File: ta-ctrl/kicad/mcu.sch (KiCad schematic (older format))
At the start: 11 parts, among them U6 MSP430FR5994IPM, Y1 Crystal, Y2 Crystal

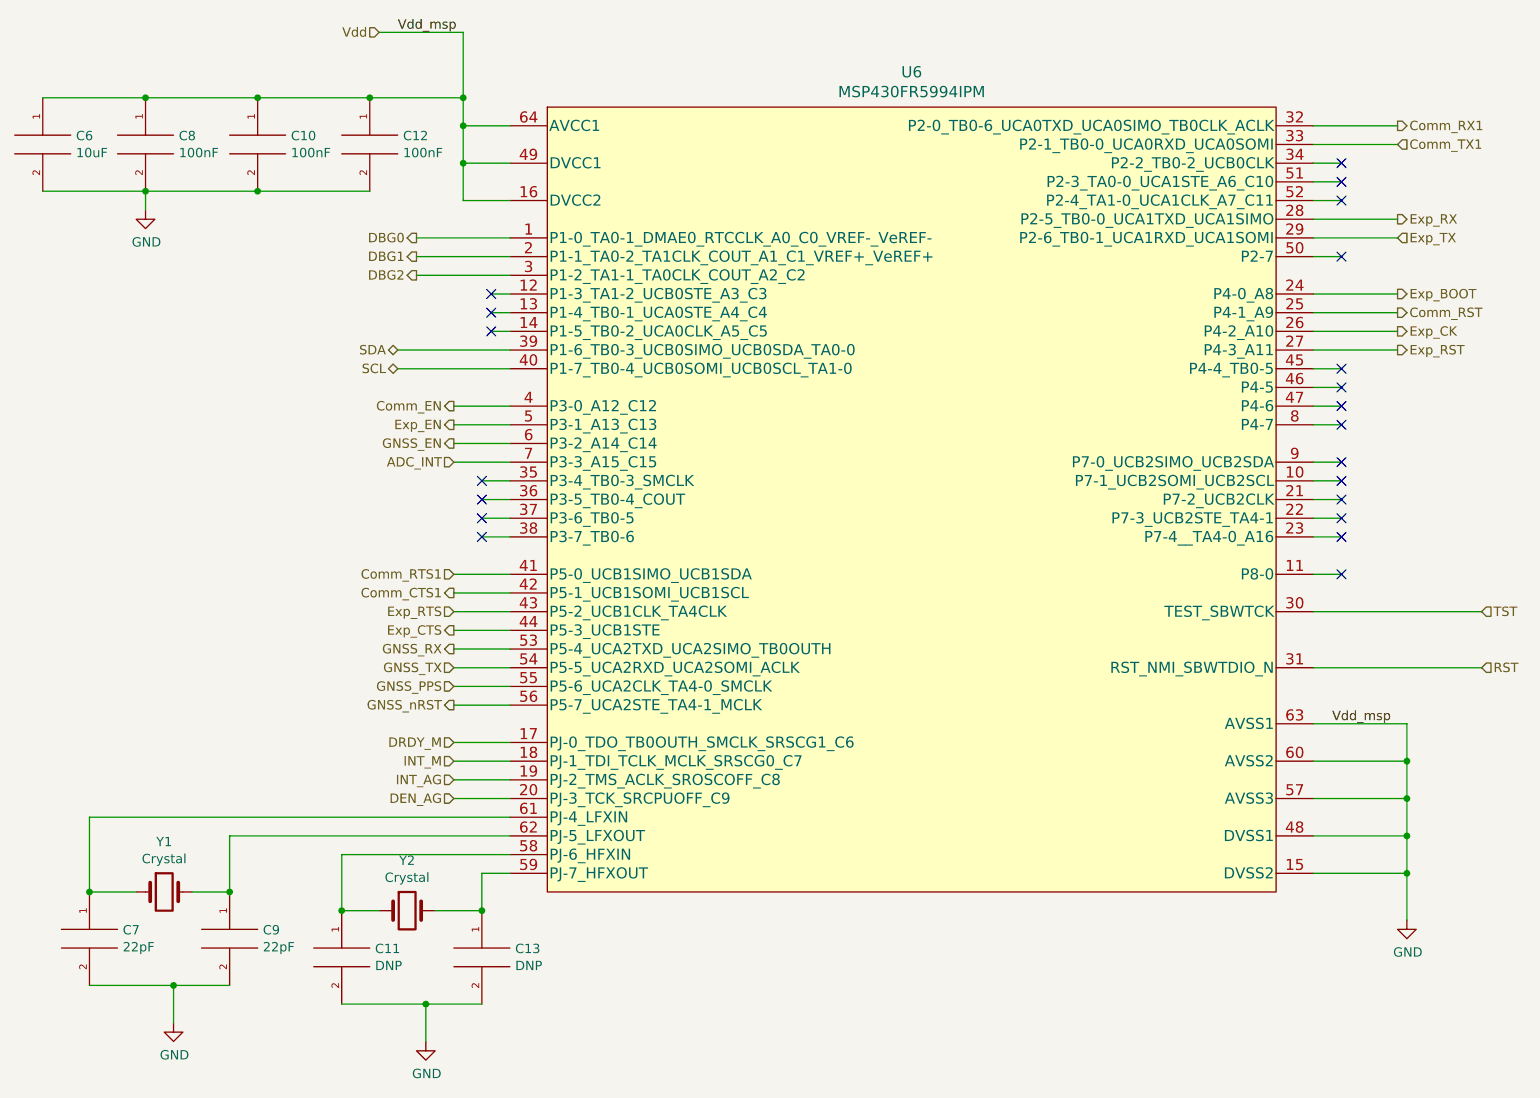
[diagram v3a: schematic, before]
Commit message: updated and checked all footprints, added a diode too
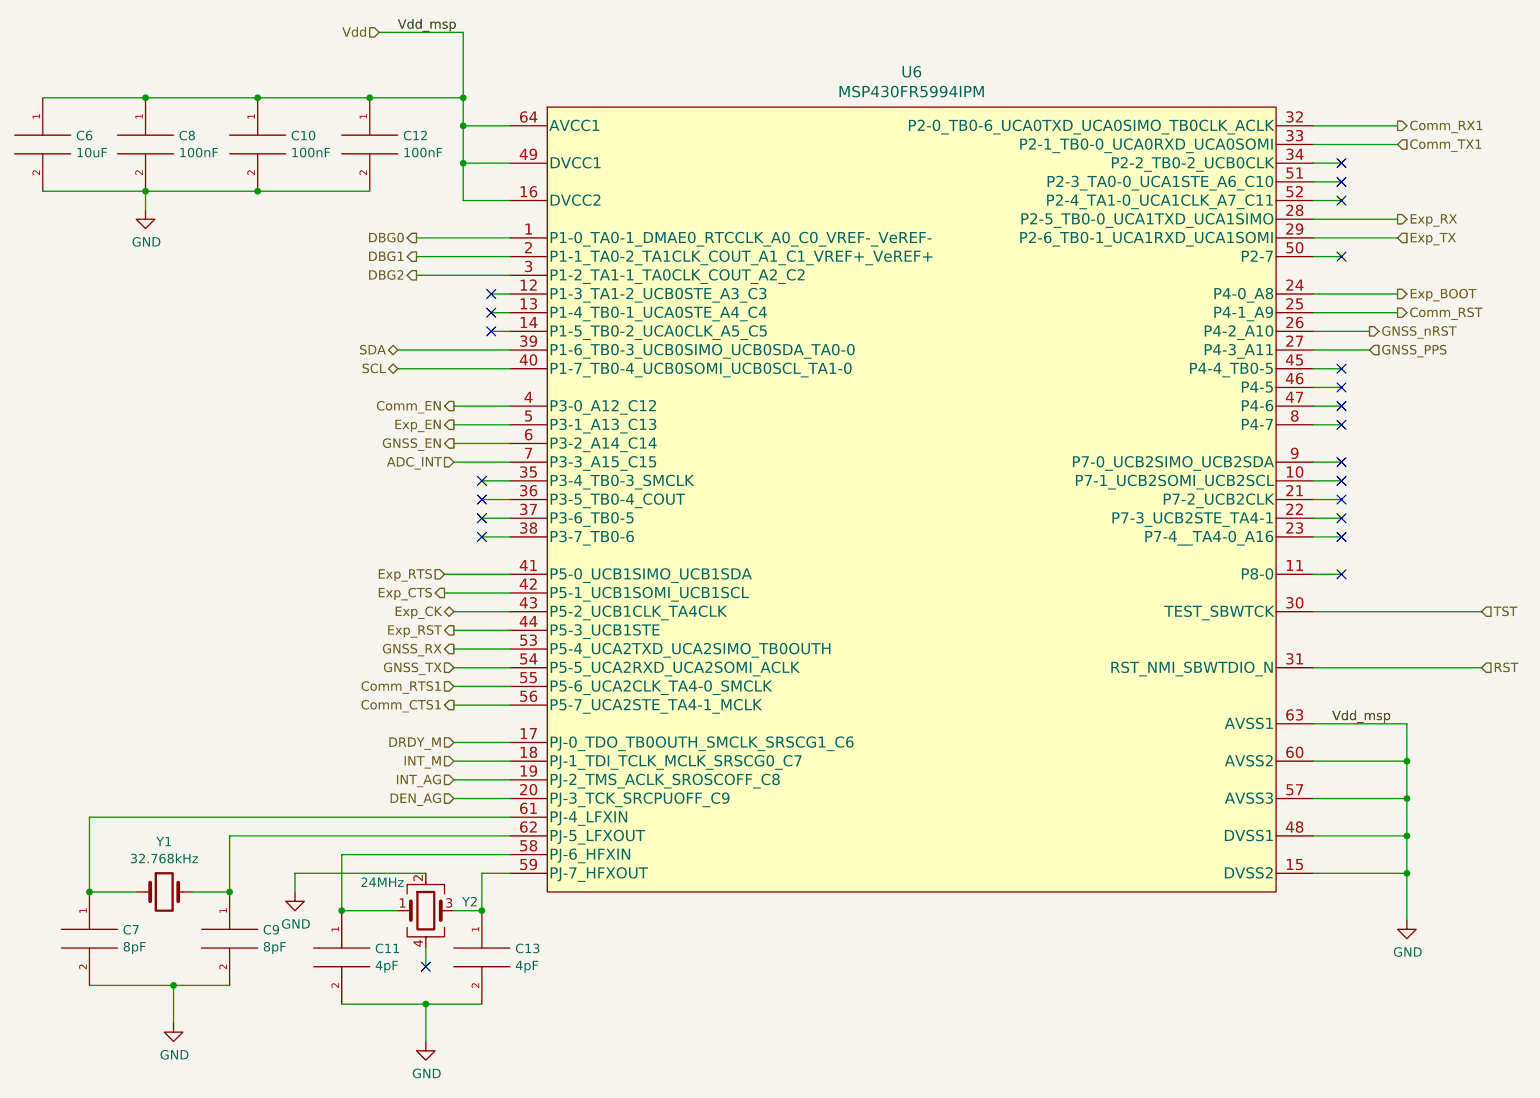
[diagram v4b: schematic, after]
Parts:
- removed Y2: Crystal, symbol Device:Crystal
- added Y2: 24MHz, ta-ctrl:ECX-1247, symbol Device:Crystal_GND24
- C10, C12, C6, C8: footprint (none) -> ta-ctrl:C_0603_1608Metric_ctrl_cpy
- C11, C13: value DNP -> 4pF; footprint (none) -> ta-ctrl:C_0402_1005Metric
- C7, C9: value 22pF -> 8pF; footprint (none) -> ta-ctrl:C_0402_1005Metric
- Y1: value Crystal -> 32.768kHz; footprint (none) -> ta-ctrl:ECS327934QSTR
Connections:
- net Comm_CTS1: now also U6.56 (P5-7_UCA2STE_TA4-1_MCLK); no longer U6.42 (P5-1_UCB1SOMI_UCB1SCL)
- net Comm_RTS1: now also U6.55 (P5-6_UCA2CLK_TA4-0_SMCLK); no longer U6.41 (P5-0_UCB1SIMO_UCB1SDA)
- net Exp_CK: now also U6.43 (P5-2_UCB1CLK_TA4CLK); no longer U6.26 (P4-2_A10)
- net Exp_CTS: now also U6.42 (P5-1_UCB1SOMI_UCB1SCL); no longer U6.44 (P5-3_UCB1STE)
- net Exp_RST: now also U6.44 (P5-3_UCB1STE); no longer U6.27 (P4-3_A11)
- net Exp_RTS: now also U6.41 (P5-0_UCB1SIMO_UCB1SDA); no longer U6.43 (P5-2_UCB1CLK_TA4CLK)
- net GND: now also Y2.2
- net GNSS_PPS: now also U6.27 (P4-3_A11); no longer U6.55 (P5-6_UCA2CLK_TA4-0_SMCLK)
- net GNSS_nRST: now also U6.26 (P4-2_A10); no longer U6.56 (P5-7_UCA2STE_TA4-1_MCLK)
- net at C11.1, U6.58 (PJ-6_HFXIN): now also Y2.1
- net at C13.1, U6.59 (PJ-7_HFXOUT): now also Y2.3
- no-connect marks 21 -> 22
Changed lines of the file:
@@
 Vdd_msp
 $Comp
-L power:GND #PWR021
+L power:GND #PWR023
 U 1 1 5F18B739
 P 8150 5800
-F 0 "#PWR021" H 8150 5550 50  0001 C CNN
+F 0 "#PWR023" H 8150 5550 50  0001 C CNN
 F 1 "GND" H 8155 5627 50  0000 C CNN
 F 2 "" H 8150 5800 50  0001 C CNN
@@
 F 0 "C8" H 1578 1696 50  0000 L CNN
 F 1 "100nF" H 1578 1605 50  0000 L CNN
-F 2 "" H 1400 1650 50  0001 C CNN
+F 2 "ta-ctrl:C_0603_1608Metric_ctrl_cpy" H 1400 1650 50  0001 C CNN
 F 3 "~" H 1400 1650 50  0001 C CNN
 	1    1400 1650
@@
 F 0 "C10" H 2178 1696 50  0000 L CNN
 F 1 "100nF" H 2178 1605 50  0000 L CNN
-F 2 "" H 2000 1650 50  0001 C CNN
+F 2 "ta-ctrl:C_0603_1608Metric_ctrl_cpy" H 2000 1650 50  0001 C CNN
 F 3 "~" H 2000 1650 50  0001 C CNN
 	1    2000 1650
@@
 F 0 "C12" H 2778 1696 50  0000 L CNN
 F 1 "100nF" H 2778 1605 50  0000 L CNN
-F 2 "" H 2600 1650 50  0001 C CNN
+F 2 "ta-ctrl:C_0603_1608Metric_ctrl_cpy" H 2600 1650 50  0001 C CNN
 F 3 "~" H 2600 1650 50  0001 C CNN
 	1    2600 1650
@@
 $EndComp
 $Comp
-L power:GND #PWR018
+L power:GND #PWR019
 U 1 1 5F18D1CF
 P 1400 2000
-F 0 "#PWR018" H 1400 1750 50  0001 C CNN
+F 0 "#PWR019" H 1400 1750 50  0001 C CNN
 F 1 "GND" H 1405 1827 50  0000 C CNN
 F 2 "" H 1400 2000 50  0001 C CNN
@@
 F 0 "C6" H 1028 1696 50  0000 L CNN
 F 1 "10uF" H 1028 1605 50  0000 L CNN
-F 2 "" H 850 1650 50  0001 C CNN
+F 2 "ta-ctrl:C_0603_1608Metric_ctrl_cpy" H 850 1650 50  0001 C CNN
 F 3 "~" H 850 1650 50  0001 C CNN
 	1    850  1650
@@
 Wire Wire Line
 	850  1900 1400 1900
-$Comp
-L Device:Crystal Y2
-U 1 1 5F187D6E
-P 2800 5750
-F 0 "Y2" H 2800 6018 50  0000 C CNN
-F 1 "Crystal" H 2800 5927 50  0000 C CNN
-F 2 "" H 2800 5750 50  0001 C CNN
-F 3 "~" H 2800 5750 50  0001 C CNN
-	1    2800 5750
-	1    0    0    -1
-$EndComp
-$Comp
-L Device:Crystal Y1
-U 1 1 5F18970C
-P 1500 5650
-F 0 "Y1" H 1500 5918 50  0000 C CNN
-F 1 "Crystal" H 1500 5827 50  0000 C CNN
-F 2 "" H 1500 5650 50  0001 C CNN
-F 3 "~" H 1500 5650 50  0001 C CNN
-	1    1500 5650
-	1    0    0    -1
-$EndComp
 $Comp
 L pspice:C C9
@@
 P 1850 5900
 F 0 "C9" H 2028 5946 50  0000 L CNN
-F 1 "22pF" H 2028 5855 50  0000 L CNN
-F 2 "" H 1850 5900 50  0001 C CNN
+F 1 "8pF" H 2028 5855 50  0000 L CNN
+F 2 "ta-ctrl:C_0402_1005Metric" H 1850 5900 50  0001 C CNN
 F 3 "~" H 1850 5900 50  0001 C CNN
 	1    1850 5900
@@
 P 1100 5900
 F 0 "C7" H 1278 5946 50  0000 L CNN
-F 1 "22pF" H 1278 5855 50  0000 L CNN
-F 2 "" H 1100 5900 50  0001 C CNN
+F 1 "8pF" H 1278 5855 50  0000 L CNN
+F 2 "ta-ctrl:C_0402_1005Metric" H 1100 5900 50  0001 C CNN
 F 3 "~" H 1100 5900 50  0001 C CNN
 	1    1100 5900
@@
 $EndComp
 $Comp
-L power:GND #PWR019
+L power:GND #PWR020
 U 1 1 5F18C345
 P 1550 6350
-F 0 "#PWR019" H 1550 6100 50  0001 C CNN
+F 0 "#PWR020" H 1550 6100 50  0001 C CNN
 F 1 "GND" H 1555 6177 50  0000 C CNN
 F 2 "" H 1550 6350 50  0001 C CNN
@@
 P 3200 6000
 F 0 "C13" H 3378 6046 50  0000 L CNN
-F 1 "DNP" H 3378 5955 50  0000 L CNN
-F 2 "" H 3200 6000 50  0001 C CNN
+F 1 "4pF" H 3378 5955 50  0000 L CNN
+F 2 "ta-ctrl:C_0402_1005Metric" H 3200 6000 50  0001 C CNN
 F 3 "~" H 3200 6000 50  0001 C CNN
 	1    3200 6000
@@
 $EndComp
 $Comp
-L pspice:C C11
-U 1 1 5F191546
-P 2450 6000
-F 0 "C11" H 2628 6046 50  0000 L CNN
-F 1 "DNP" H 2628 5955 50  0000 L CNN
-F 2 "" H 2450 6000 50  0001 C CNN
-F 3 "~" H 2450 6000 50  0001 C CNN
-	1    2450 6000
-	1    0    0    -1
-$EndComp
-$Comp
-L power:GND #PWR020
+L power:GND #PWR022
 U 1 1 5F19154C
 P 2900 6450
-F 0 "#PWR020" H 2900 6200 50  0001 C CNN
+F 0 "#PWR022" H 2900 6200 50  0001 C CNN
 F 1 "GND" H 2905 6277 50  0000 C CNN
 F 2 "" H 2900 6450 50  0001 C CNN
@@
 	2900 6250 3200 6250
 Wire Wire Line
-	2450 5750 2650 5750
-Wire Wire Line
-	2950 5750 3200 5750
-Wire Wire Line
 	2450 5750 2450 5450
 Wire Wire Line
 	2450 5450 3350 5450
-Connection ~ 2450 5750
 Wire Wire Line
 	3200 5750 3200 5550
 Wire Wire Line
 	3200 5550 3350 5550
-Connection ~ 3200 5750
 Text HLabel 8550 4150 2    50   Input ~ 0
 TST
@@
 Text HLabel 8100 2150 2    50   Input ~ 0
 Exp_TX
-Text HLabel 3050 4250 0    50   Output ~ 0
+Text HLabel 3000 4050 0    50   Output ~ 0
 Exp_CTS
 Text HLabel 3050 4350 0    50   Output ~ 0
@@
 Text HLabel 3050 4450 0    50   Input ~ 0
 GNSS_TX
-Text HLabel 3050 4650 0    50   Output ~ 0
+Text HLabel 7950 2650 2    50   Output ~ 0
 GNSS_nRST
-Text HLabel 3050 4550 0    50   Input ~ 0
+Text HLabel 7950 2750 2    50   Input ~ 0
 GNSS_PPS
 Text HLabel 2750 2750 0    50   BiDi ~ 0
@@
 	3350 4450 3050 4450
 Wire Wire Line
+	7950 2750 7650 2750
+Wire Wire Line
+	7950 2650 7650 2650
+Wire Wire Line
 	3050 4550 3350 4550
 Wire Wire Line
 	3050 4650 3350 4650
-Wire Wire Line
-	3050 3950 3350 3950
-Wire Wire Line
-	3050 4050 3350 4050
 Wire Wire Line
 	3050 4150 3350 4150
@@
 Wire Wire Line
 	7650 2550 8100 2550
-Text HLabel 8100 2650 2    50   Output ~ 0
+Text HLabel 3050 4150 0    50   BiDi ~ 0
 Exp_CK
-Text HLabel 8100 2750 2    50   Output ~ 0
+Text HLabel 3050 4250 0    50   Output ~ 0
 Exp_RST
-Wire Wire Line
-	7650 2650 8100 2650
-Wire Wire Line
-	7650 2750 8100 2750
 Text HLabel 3050 4850 0    50   Input ~ 0
 DRDY_M
@@
 Wire Wire Line
 	3050 4850 3350 4850
-Text HLabel 3050 4150 0    50   Input ~ 0
+Text HLabel 3000 3950 0    50   Input ~ 0
 Exp_RTS
-Text HLabel 3050 4050 0    50   Output ~ 0
+Text HLabel 3050 4650 0    50   Output ~ 0
 Comm_CTS1
-Text HLabel 3050 3950 0    50   Input ~ 0
+Text HLabel 3050 4550 0    50   Input ~ 0
 Comm_RTS1
 NoConn ~ 3200 3450
@@
 Wire Wire Line
 	7650 3950 7800 3950
+Wire Wire Line
+	3000 4050 3350 4050
+Wire Wire Line
+	3000 3950 3350 3950
+$Comp
+L Device:Crystal Y1
+U 1 1 5F1B1D55
+P 1500 5650
+F 0 "Y1" H 1500 5918 50  0000 C CNN
+F 1 "32.768kHz" H 1500 5827 50  0000 C CNN
+F 2 "ta-ctrl:ECS327934QSTR" H 1500 5650 50  0001 C CNN
+F 3 "~" H 1500 5650 50  0001 C CNN
+	1    1500 5650
+	1    0    0    -1
+$EndComp
+$Comp
+L Device:Crystal_GND24 Y2
+U 1 1 5F1B3506
+P 2900 5750
+F 0 "Y2" H 3094 5796 50  0000 L CNN
+F 1 "24MHz" H 2550 5900 50  0000 L CNN
+F 2 "ta-ctrl:ECX-1247" H 2900 5750 50  0001 C CNN
+F 3 "https://www.mouser.com/datasheet/2/122/ECX-1247Q-1388650.pdf" H 2900 5750 50  0001 C CNN
+F 4 "ECS-240-10-47Q-CES-TR" H 2900 5750 50  0001 C CNN "Manufacturer Part Number"
+F 5 "Mouser" H 2900 5750 50  0001 C CNN "Vendor"
+F 6 "520-240-10-47Q-CEST" H 2900 5750 50  0001 C CNN "Vendor Part Number"
+	1    2900 5750
+	1    0    0    -1
+$EndComp
+$Comp
+L pspice:C C11
+U 1 1 5F191546
+P 2450 6000
+F 0 "C11" H 2628 6046 50  0000 L CNN
+F 1 "4pF" H 2628 5955 50  0000 L CNN
+F 2 "ta-ctrl:C_0402_1005Metric" H 2450 6000 50  0001 C CNN
+F 3 "~" H 2450 6000 50  0001 C CNN
+	1    2450 6000
+	1    0    0    -1
+$EndComp
+Wire Wire Line
+	3050 5750 3200 5750
+Connection ~ 3200 5750
+Wire Wire Line
+	2750 5750 2450 5750
+Connection ~ 2450 5750
+Wire Wire Line
+	2900 5550 2200 5550
+Wire Wire Line
+	2200 5550 2200 5650
+$Comp
+L power:GND #PWR021
+U 1 1 5F1C86BF
+P 2200 5650
+F 0 "#PWR021" H 2200 5400 50  0001 C CNN
+F 1 "GND" H 2205 5477 50  0000 C CNN
+F 2 "" H 2200 5650 50  0001 C CNN
+F 3 "" H 2200 5650 50  0001 C CNN
+	1    2200 5650
+	1    0    0    -1
+$EndComp
+NoConn ~ 2900 6050
+Wire Wire Line
+	2900 5950 2900 6050
 $EndSCHEMATC

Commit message: all parts placed, about halfway through routing
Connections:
- net DEN_AG: now also U6.17 (PJ-0_TDO_TB0OUTH_SMCLK_SRSCG1_C6); no longer U6.20 (PJ-3_TCK_SRCPUOFF_C9)
- net DRDY_M: now also U6.20 (PJ-3_TCK_SRCPUOFF_C9); no longer U6.17 (PJ-0_TDO_TB0OUTH_SMCLK_SRSCG1_C6)
- net Exp_CK: now also U6.21 (P7-2_UCB2CLK); no longer U6.43 (P5-2_UCB1CLK_TA4CLK)
- net Exp_CTS: now also U6.10 (P7-1_UCB2SOMI_UCB2SCL); no longer U6.42 (P5-1_UCB1SOMI_UCB1SCL)
- net Exp_RTS: now also U6.9 (P7-0_UCB2SIMO_UCB2SDA); no longer U6.41 (P5-0_UCB1SIMO_UCB1SDA)
- net GND: no longer C10.1, C12.1, C6.1, C8.1, U6.16 (DVCC2), U6.49 (DVCC1), U6.64 (AVCC1)
- net INT_AG: now also U6.18 (PJ-1_TDI_TCLK_MCLK_SRSCG0_C7); no longer U6.19 (PJ-2_TMS_ACLK_SROSCOFF_C8)
- net INT_M: now also U6.19 (PJ-2_TMS_ACLK_SROSCOFF_C8); no longer U6.18 (PJ-1_TDI_TCLK_MCLK_SRSCG0_C7)
- new net Vdd: C10.1, C12.1, C6.1, C8.1, U6.16 (DVCC2), U6.49 (DVCC1), U6.64 (AVCC1)
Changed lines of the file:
@@
 Text Label 2750 1050 0    50   ~ 0
-Vdd_msp
-Text Label 7750 4750 0    50   ~ 0
 Vdd_msp
 $Comp
@@
 Text HLabel 8100 2150 2    50   Input ~ 0
 Exp_TX
-Text HLabel 3000 4050 0    50   Output ~ 0
-Exp_CTS
 Text HLabel 3050 4350 0    50   Output ~ 0
 GNSS_RX
@@
 	3050 4650 3350 4650
 Wire Wire Line
-	3050 4150 3350 4150
-Wire Wire Line
 	3050 4250 3350 4250
 Text HLabel 3050 3050 0    50   Output ~ 0
@@
 Wire Wire Line
 	7650 2550 8100 2550
-Text HLabel 3050 4150 0    50   BiDi ~ 0
-Exp_CK
 Text HLabel 3050 4250 0    50   Output ~ 0
 Exp_RST
+Text HLabel 3050 5150 0    50   Input ~ 0
+DRDY_M
+Text HLabel 3050 5050 0    50   Input ~ 0
+INT_M
+Text HLabel 3050 4950 0    50   Input ~ 0
+INT_AG
 Text HLabel 3050 4850 0    50   Input ~ 0
-DRDY_M
-Text HLabel 3050 4950 0    50   Input ~ 0
-INT_M
-Text HLabel 3050 5050 0    50   Input ~ 0
-INT_AG
-Text HLabel 3050 5150 0    50   Input ~ 0
 DEN_AG
 Wire Wire Line
+	3050 4850 3350 4850
+Wire Wire Line
+	3050 4950 3350 4950
+Wire Wire Line
+	3050 5050 3350 5050
+Wire Wire Line
 	3050 5150 3350 5150
-Wire Wire Line
-	3050 5050 3350 5050
-Wire Wire Line
-	3050 4950 3350 4950
-Wire Wire Line
-	3050 4850 3350 4850
-Text HLabel 3000 3950 0    50   Input ~ 0
-Exp_RTS
 Text HLabel 3050 4650 0    50   Output ~ 0
 Comm_CTS1
@@
 Wire Wire Line
 	7650 3150 7800 3150
-NoConn ~ 7800 3350
-NoConn ~ 7800 3450
-NoConn ~ 7800 3550
 NoConn ~ 7800 3650
 NoConn ~ 7800 3750
 Wire Wire Line
-	7650 3350 7800 3350
-Wire Wire Line
-	7650 3450 7800 3450
-Wire Wire Line
-	7650 3550 7800 3550
-Wire Wire Line
 	7650 3650 7800 3650
 Wire Wire Line
@@
 Wire Wire Line
 	7650 3950 7800 3950
-Wire Wire Line
-	3000 4050 3350 4050
-Wire Wire Line
-	3000 3950 3350 3950
 $Comp
 L Device:Crystal Y1
@@
 Wire Wire Line
 	2900 5950 2900 6050
+Text HLabel 8150 3350 2    50   Input ~ 0
+Exp_RTS
+Text HLabel 8100 3550 2    50   BiDi ~ 0
+Exp_CK
+Text HLabel 8150 3450 2    50   Output ~ 0
+Exp_CTS
+Wire Wire Line
+	7650 3350 8150 3350
+Wire Wire Line
+	7650 3450 8150 3450
+Wire Wire Line
+	7650 3550 8100 3550
+NoConn ~ 3200 4150
+NoConn ~ 3200 4050
+NoConn ~ 3200 3950
+Wire Wire Line
+	3350 4150 3200 4150
+Wire Wire Line
+	3350 4050 3200 4050
+Wire Wire Line
+	3350 3950 3200 3950
 $EndSCHEMATC
